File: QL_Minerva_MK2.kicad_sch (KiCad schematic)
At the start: 16 parts, among them J1 Conn_01x02_Pin, J2 Conn_01x05_Pin, U1 Socket to QL, U2 W27C512, U3 PCF8583P, U4 GAL16V8, U5 74LS133, Y1 32.768 kHz

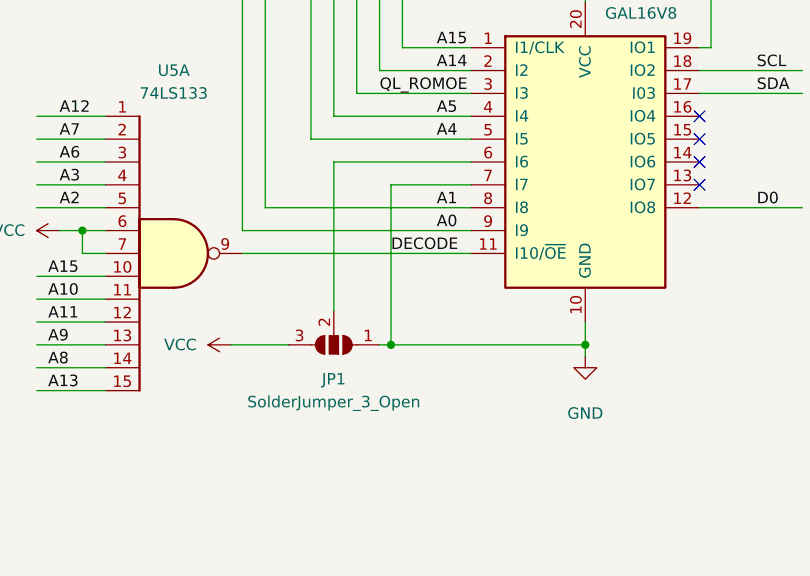
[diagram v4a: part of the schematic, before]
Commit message: fixed error in leg 7 of gal
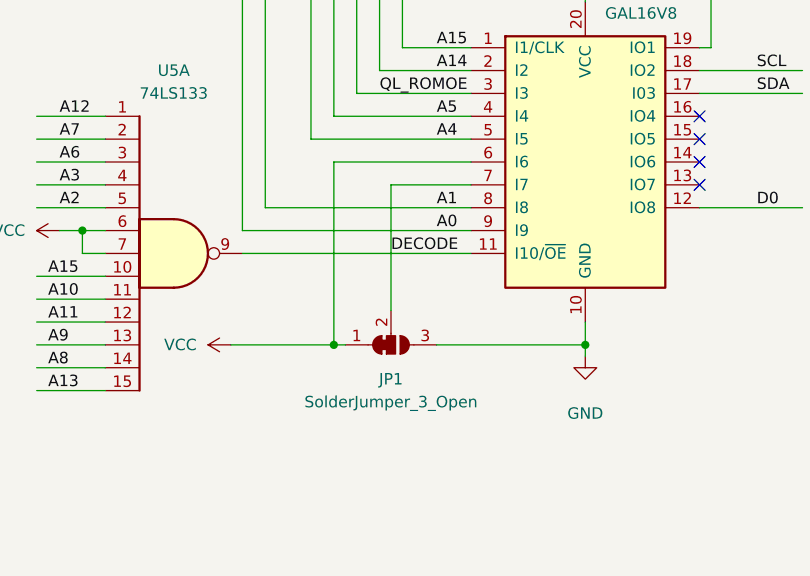
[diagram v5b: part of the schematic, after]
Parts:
- C1: footprint Capacitor_THT:CP_Radial_D4.0mm_P1.50mm -> 8bits:C_Variable_Radial_D6.0mm_P5.00mm
- JP1: footprint Jumper:SolderJumper-3_P1.3mm_Open_RoundedPad1.0x1.5mm -> Jumper:SolderJumper-3_P1.3mm_Bridged12_RoundedPad1.0x1.5mm; symbol Jumper:SolderJumper_3_Open -> Jumper:SolderJumper_3_Bridged12; now left out of the parts list
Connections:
- net GND: now also JP1.3 (B); no longer JP1.1 (A), U4.11 (I10/~{OE}), U4.7 (I7), U5.9
- net VCC: now also JP1.1 (A), U4.6 (I6); no longer JP1.3 (B)
- net DECODE: now reaches JP1.2 (C)
- net DECODE: now also U4.11 (I10/~{OE}), U4.7 (I7), U5.9; no longer U4.6 (I6)
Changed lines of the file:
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@@
 	(title_block
 		(title "Minerva MK II Reimagined")
-		(date "2025-02-23")
-		(rev "0.1")
+		(date "2025-04-08")
+		(rev "0.2")
 		(company "Alvaro Alea Fernandez")
 	)
@@
 	)
 	(junction
+		(at 99.06 160.02)
+		(diameter 0)
+		(color 0 0 0 0)
+	)
+	(junction
 		(at 195.58 55.88)
 		(diameter 0)
@@
 	)
 	(junction
-		(at 78.74 87.63)
+		(at 71.12 160.02)
 		(diameter 0)
 		(color 0 0 0 0)
 	)
 	(junction
-		(at 139.7 158.75)
+		(at 78.74 87.63)
 		(diameter 0)
 		(color 0 0 0 0)
 	)
 	(junction
-		(at 71.12 52.07)
+		(at 139.7 158.75)
 		(diameter 0)
 		(color 0 0 0 0)
 	)
 	(junction
-		(at 99.06 160.02)
+		(at 71.12 52.07)
 		(diameter 0)
 		(color 0 0 0 0)
@@
 	)
 	(junction
-		(at 77.47 160.02)
-		(diameter 0)
-		(color 0 0 0 0)
-	)
-	(junction
 		(at 139.7 186.69)
 		(diameter 0)
@@
 	(wire
 		(pts
+			(xy 71.12 160.02) (xy 72.39 160.02)
+		)
+		(stroke
+			(width 0)
+			(type default)
+		)
+	)
+	(wire
+		(pts
 			(xy 38.1 144.78) (xy 45.72 144.78)
 		)
@@
 	(wire
 		(pts
-			(xy 99.06 161.29) (xy 99.06 160.02)
+			(xy 151.13 39.37) (xy 139.7 39.37)
 		)
 		(stroke
@@
 	(wire
 		(pts
-			(xy 151.13 39.37) (xy 139.7 39.37)
+			(xy 38.1 139.7) (xy 45.72 139.7)
 		)
 		(stroke
@@
 	(wire
 		(pts
-			(xy 38.1 139.7) (xy 45.72 139.7)
+			(xy 82.55 160.02) (xy 99.06 160.02)
 		)
 		(stroke
@@
 	(wire
 		(pts
+			(xy 71.12 139.7) (xy 71.12 160.02)
+		)
+		(stroke
+			(width 0)
+			(type default)
+		)
+	)
+	(wire
+		(pts
 			(xy 229.87 22.86) (xy 229.87 24.13)
 		)
@@
 	(wire
 		(pts
-			(xy 77.47 142.24) (xy 77.47 160.02)
+			(xy 77.47 142.24) (xy 77.47 156.21)
 		)
 		(stroke
@@
 	(wire
 		(pts
-			(xy 77.47 160.02) (xy 99.06 160.02)
-		)
-		(stroke
-			(width 0)
-			(type default)
-		)
-	)
-	(wire
-		(pts
 			(xy 151.13 52.07) (xy 139.7 52.07)
 		)
@@
 	(wire
 		(pts
-			(xy 59.69 160.02) (xy 66.04 160.02)
+			(xy 59.69 160.02) (xy 71.12 160.02)
 		)
 		(stroke
@@
 		)
 	)
-	(wire
-		(pts
-			(xy 76.2 160.02) (xy 77.47 160.02)
-		)
-		(stroke
-			(width 0)
-			(type default)
-		)
-	)
 	(bus
 		(pts
@@
 	(wire
 		(pts
-			(xy 71.12 139.7) (xy 71.12 156.21)
+			(xy 151.13 41.91) (xy 139.7 41.91)
 		)
 		(stroke
@@
 		)
 	)
-	(wire
+	(bus
 		(pts
-			(xy 151.13 41.91) (xy 139.7 41.91)
+			(xy 21.59 36.83) (xy 21.59 39.37)
 		)
 		(stroke
@@
 		)
 	)
-	(bus
+	(wire
 		(pts
-			(xy 21.59 36.83) (xy 21.59 39.37)
+			(xy 99.06 160.02) (xy 99.06 161.29)
 		)
 		(stroke
@@
 	)
 	(symbol
-		(lib_id "Jumper:SolderJumper_3_Open")
-		(at 71.12 160.02 180)
+		(lib_id "Jumper:SolderJumper_3_Bridged12")
+		(at 77.47 160.02 0)
+		(mirror x)
 		(unit 1)
 		(exclude_from_sim no)
-		(in_bom yes)
+		(in_bom no)
 		(on_board yes)
 		(dnp no)
-		(fields_autoplaced yes)
 		(property "Reference" "JP1"
-			(at 71.12 163.83 0)
+			(at 77.47 163.83 0)
 			(effects
 				(font
@@
 		)
 		(property "Value" "SolderJumper_3_Open"
-			(at 71.12 166.37 0)
+			(at 77.47 166.37 0)
 			(effects
 				(font
@@
 			)
 		)
-		(property "Footprint" "Jumper:SolderJumper-3_P1.3mm_Open_RoundedPad1.0x1.5mm"
-			(at 71.12 160.02 0)
+		(property "Footprint" "Jumper:SolderJumper-3_P1.3mm_Bridged12_RoundedPad1.0x1.5mm"
+			(at 77.47 160.02 0)
 			(effects
 				(font
@@
 		)
 		(property "Datasheet" "~"
-			(at 71.12 160.02 0)
+			(at 77.47 160.02 0)
 			(effects
 				(font
@@
 			)
 		)
-		(property "Description" ""
-			(at 71.12 160.02 0)
+		(property "Description" "3-pole Solder Jumper, pins 1+2 closed/bridged"
+			(at 77.47 160.02 0)
 			(effects
 				(font
@@
 			)
 		)
-		(property "Footprint" "Capacitor_THT:CP_Radial_D4.0mm_P1.50mm"
+		(property "Footprint" "8bits:C_Variable_Radial_D6.0mm_P5.00mm"
 			(at 196.85 66.04 0)
 			(effects
